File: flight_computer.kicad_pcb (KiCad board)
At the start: 2 copper layers, 43 x 60 mm, 10 parts, among them J1 Conn_01x13_Socket, J2 Conn_01x13_Socket, J3 Ignitor Output, J4 9v Battery Input, U1 CPC1002N, U2 CPC1002N, U3 CPC1002N

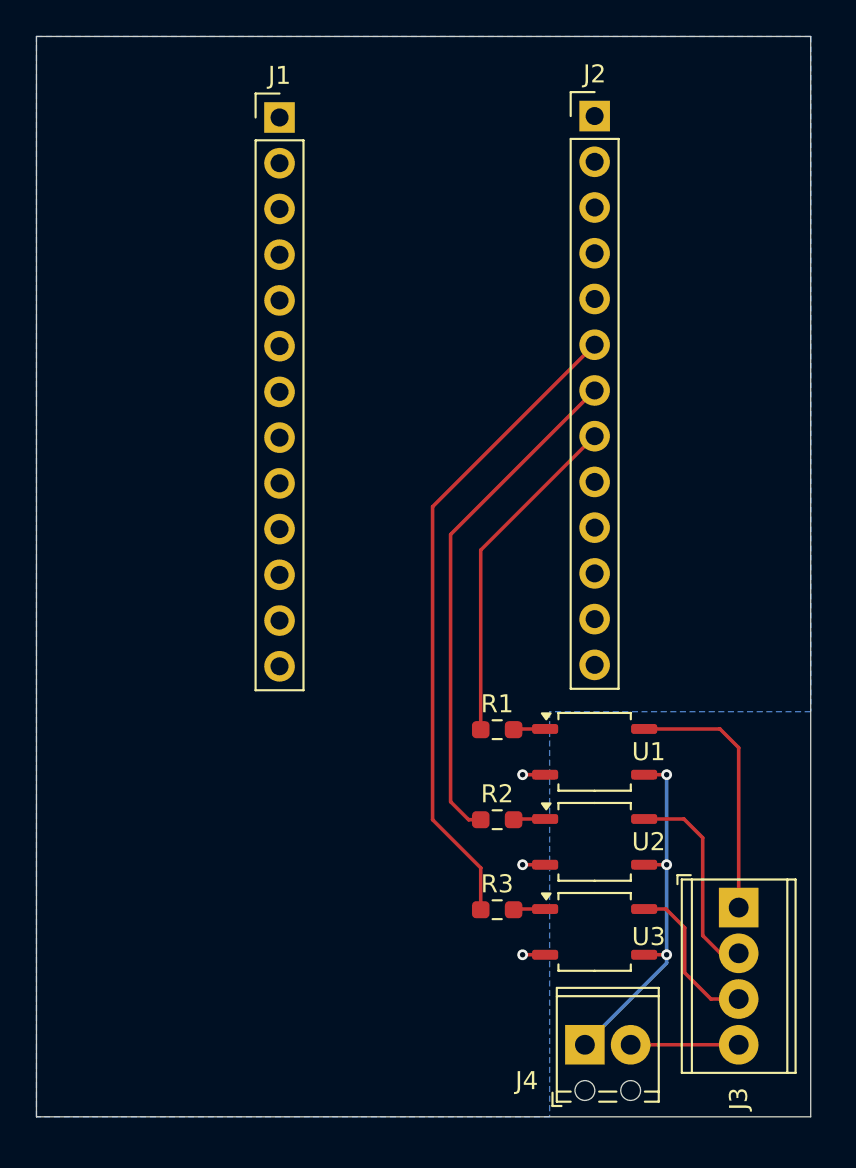
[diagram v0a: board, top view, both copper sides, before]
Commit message: Layout finished for BNO055 and BME280
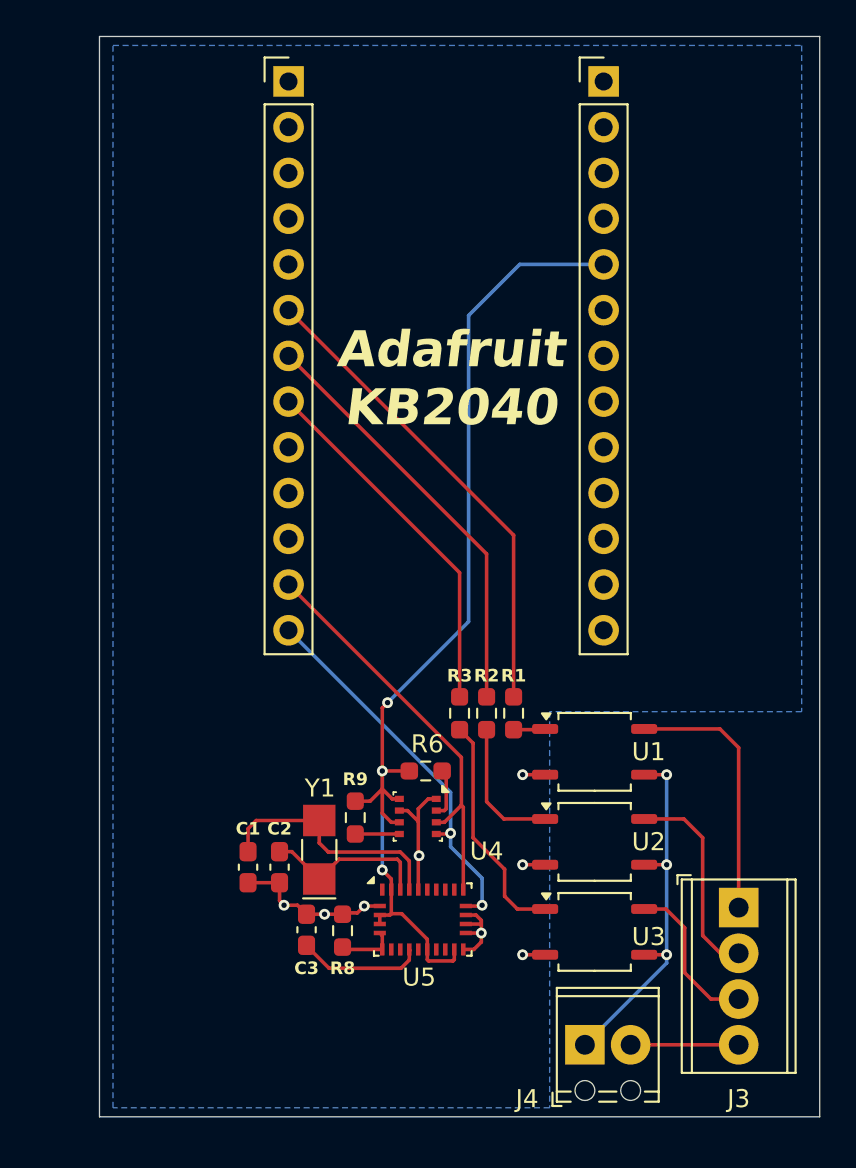
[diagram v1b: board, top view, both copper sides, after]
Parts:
- added C1: 22pF, Capacitor_SMD:C_0603_1608Metric_Pad1.08x0.95mm_HandSolder, F.Cu at (96.8, 104.6)
- added C2: 22pF, Capacitor_SMD:C_0603_1608Metric_Pad1.08x0.95mm_HandSolder, F.Cu at (98.5, 104.6)
- added C3: 0.1µF, Capacitor_SMD:C_0603_1608Metric_Pad1.08x0.95mm_HandSolder, F.Cu at (100.0, 108.1)
- added R6: 10k, Resistor_SMD:R_0603_1608Metric_Pad0.98x0.95mm_HandSolder, F.Cu at (106.6, 99.3)
- added R8: 10k, Resistor_SMD:R_0603_1608Metric_Pad0.98x0.95mm_HandSolder, F.Cu at (102.0, 108.2)
- added R9: 10k, Resistor_SMD:R_0603_1608Metric_Pad0.98x0.95mm_HandSolder, F.Cu at (102.7, 101.9)
- added U4: BME280, Package_LGA:Bosch_LGA-8_2.5x2.5mm_P0.65mm_ClockwisePinNumbering, F.Cu at (106.2, 101.8)
- added U5: BNO055, Package_LGA:LGA-28_5.2x3.8mm_P0.5mm, F.Cu at (106.5, 107.5)
- added Y1: 33.768kHz, Crystal:Crystal_SMD_G8-2Pin_3.2x1.5mm_HandSoldering, F.Cu at (100.7, 103.7)
- moved J1 18.1 mm to (116.5, 61.0)
- moved J2 17.1 mm to (99.0, 61.0)
- moved R3 11.1 mm to (108.5, 96.1), turned to -90 degrees
- moved R2 5.94 mm to (110.0, 96.1), turned to -90 degrees
- moved R1 1.29 mm to (111.5, 96.1), turned to -90 degrees
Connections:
- net Ignitor Logic 2 + renamed /Ignitor Logic 2 +
- net Ignitor Terminal 1 renamed /Ignitor Terminal 1
- net Ignitor Terminal 2 renamed /Ignitor Terminal 2
- net Ignitor Terminal 3 renamed /Ignitor Terminal 3
- net Ignitor Terminal Common renamed /Ignitor Terminal GND
- J1 pad 5: unconnected-(J1-Pin_5-Pad5) -> +3.3V
- J2 pad 12: unconnected-(J2-Pin_12-Pad12) -> /SDA
- J2 pad 13: unconnected-(J2-Pin_13-Pad13) -> /SCL
- J2 pad 6: Ignitor Logic 3 + -> /Ignitor Logic 1 +
- J2 pad 8: Ignitor Logic 1 + -> /Ignitor Logic 3 +
- R1 pad 1: Ignitor Logic 1 + -> /Ignitor Logic 1 +
- R3 pad 1: Ignitor Logic 3 + -> /Ignitor Logic 3 +
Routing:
- net +3.3V: track 0.00 -> 59.1 mm, vias 0 -> 3
- net Ignitor Logic 3 +: track 36.2 -> 0.00 mm
- net /Ignitor Logic 1 +: track 0.00 -> 26.7 mm
- net /SDA: track 0.00 -> 22.7 mm
- net /SCL: track 0.00 -> 21.5 mm, vias 0 -> 2
- net GND: track 3.75 -> 24.7 mm, vias 3 -> 8
- net /Ignitor Logic 3 +: track 0.00 -> 20.3 mm
- net Ignitor Logic 1 +: track 18.9 -> 0.00 mm
- net Net-(U5-XOUT32): track 0.00 -> 13.7 mm
- net Net-(R3-Pad2): track 1.77 -> 12.9 mm
- net Net-(U5-XIN32): track 0.00 -> 9.38 mm
- net Net-(U5-CAP): track 0.00 -> 7.09 mm
- net Net-(R2-Pad2): track 1.77 -> 7.70 mm
- net /Ignitor Logic 2 +: track 28.2 -> 23.5 mm
- net Net-(U5-PS0): track 0.00 -> 3.30 mm
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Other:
- board size 43 x 60 mm -> 40 x 60 mm
- board text added: "Adafruit KB2040"

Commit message: Completed sensor layout
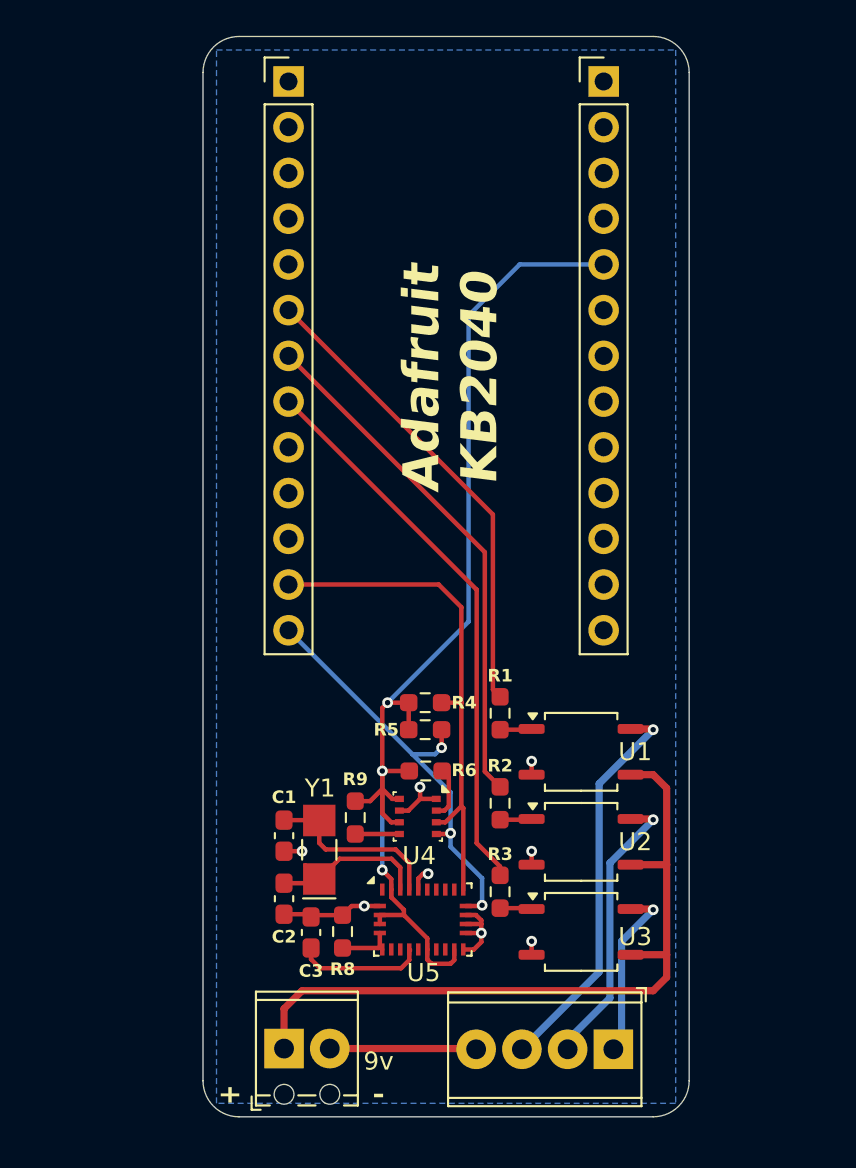
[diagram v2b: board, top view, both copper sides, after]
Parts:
- added R4: 4.4k, Resistor_SMD:R_0603_1608Metric_Pad0.98x0.95mm_HandSolder, F.Cu at (106.6, 95.5)
- added R5: 4.4k, Resistor_SMD:R_0603_1608Metric_Pad0.98x0.95mm_HandSolder, F.Cu at (106.6, 97.0)
- moved J4 16.7 mm to (98.8, 114.7)
- moved J3 10.5 mm to (117.0, 114.8), turned to 180 degrees
- moved R3 10.2 mm to (110.8, 106.0)
- moved R2 5.06 mm to (110.8, 101.1)
- moved C1 2.66 mm to (98.8, 102.9)
- moved C2 1.77 mm to (98.8, 106.4)
- moved R1 0.75 mm to (110.8, 96.1)
- moved U1 0.75 mm to (115.2, 98.2)
- moved U2 0.75 mm to (115.2, 103.2)
- moved U3 0.75 mm to (115.2, 108.2)
- moved C3 0.29 mm to (100.2, 108.3)
- moved R8 0.05 mm to (102.0, 108.2)
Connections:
- net /Ignitor Terminal GND renamed /Ignitor Terminal +
- J3 pad 1: /Ignitor Terminal 1 -> /Ignitor Terminal 3
- J3 pad 3: /Ignitor Terminal 3 -> /Ignitor Terminal 1
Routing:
- net /Ignitor Terminal +: track 16.9 -> 41.0 mm, vias 3 -> 0
- net Net-(R3-Pad2): track 12.9 -> 1.77 mm
- net /Ignitor Logic 3 +: track 20.3 -> 31.2 mm
- net /Ignitor Terminal 1: track 14.6 -> 22.0 mm, vias 0 -> 1
- net GND: track 24.7 -> 18.2 mm
- net /SDA: track 22.7 -> 28.7 mm
- net Net-(R2-Pad2): track 7.70 -> 1.77 mm
- net /Ignitor Logic 2 +: track 23.5 -> 28.8 mm
- net /Ignitor Terminal 2: track 11.5 -> 16.0 mm, vias 0 -> 1
- net Net-(U5-XOUT32): track 13.7 -> 10.1 mm
- net +3.3V: track 59.1 -> 62.2 mm
- net /SCL: track 21.5 -> 24.2 mm, vias 2 -> 3
- net Net-(J3-Pin_4): track 6.00 -> 8.15 mm
- net /Ignitor Terminal 3: track 8.79 -> 9.93 mm, vias 0 -> 1
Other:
- board size 40 x 60 mm -> 27 x 60 mm
- board text added: "+"
- board text added: "-"
- board text added: "9v"
- board text added: "Revision: 0.1.0"
- board text added: "UNL Aerospace Flight Computer"

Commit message: Added voltage regulator
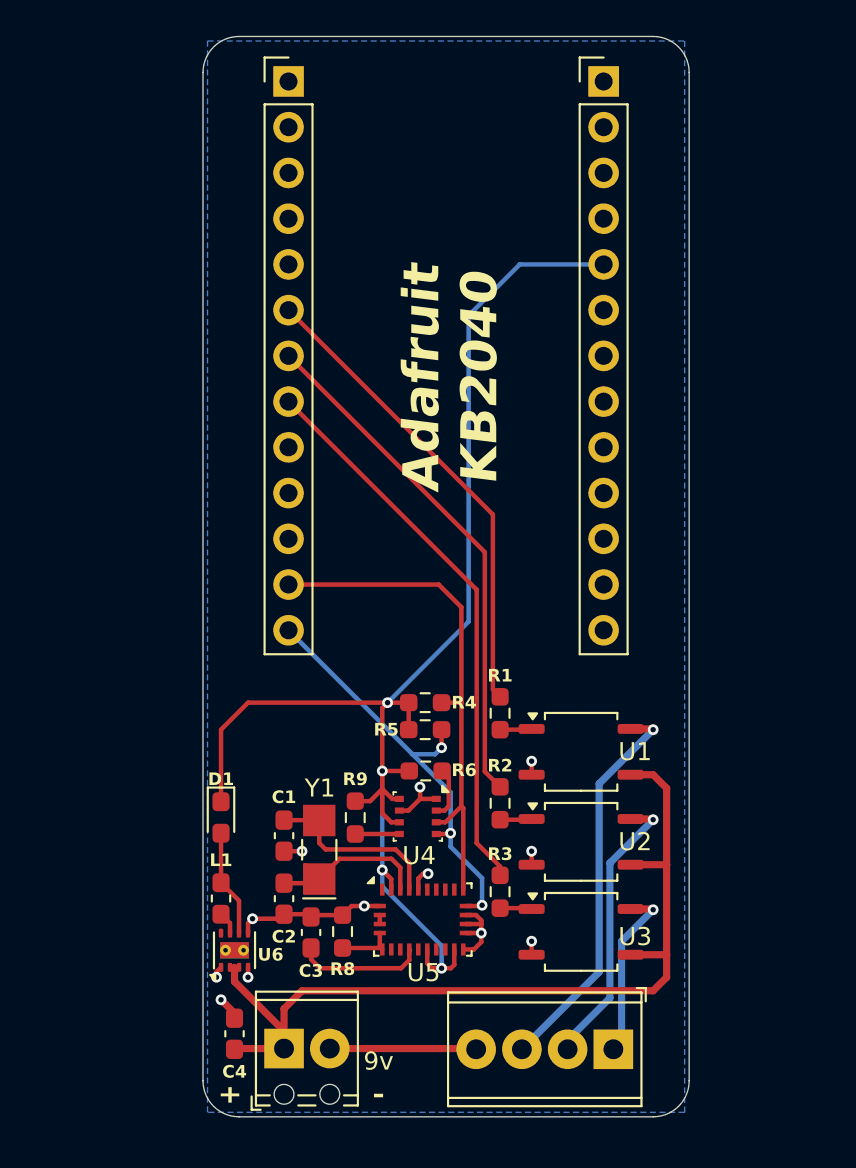
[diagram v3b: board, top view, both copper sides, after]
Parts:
- added C4: 10µF, Capacitor_SMD:C_0603_1608Metric_Pad1.08x0.95mm_HandSolder, F.Cu at (96.0, 113.9)
- added D1: D, Diode_SMD:D_0603_1608Metric_Pad1.05x0.95mm_HandSolder, F.Cu at (95.2, 101.9)
- added L1: 2.2µH, Inductor_SMD:L_0603_1608Metric_Pad1.05x0.95mm_HandSolder, F.Cu at (95.2, 106.4)
- added U6: TPS62172DSG, Package_SON:WSON-8-1EP_2x2mm_P0.5mm_EP0.9x1.6mm_ThermalVias, F.Cu at (96.0, 109.2)
- J4: value 9v Battery Input -> Battery Input
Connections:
- net /Ignitor Terminal + renamed +BATT
- J1 pad 2: unconnected-(J1-Pin_2-Pad2) -> +3.3V
- J1 pad 5: +3.3V -> unconnected-(J1-Pin_5-Pad5)
- J3 pad 4: Net-(J3-Pin_4) -> GND
- J4 pad 2: Net-(J3-Pin_4) -> GND
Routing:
- net +3.3V: track 62.2 -> 77.7 mm, vias 3 -> 4
- net GND: track 18.2 -> 31.7 mm, vias 8 -> 12
- net +BATT: track 41.0 -> 49.9 mm
- net Net-(J3-Pin_4): track 8.15 -> 0.00 mm
- net Net-(D1-A): track 0.00 -> 6.21 mm
- net Net-(U6-SW): track 0.00 -> 1.26 mm

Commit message: Improved layout of connectors
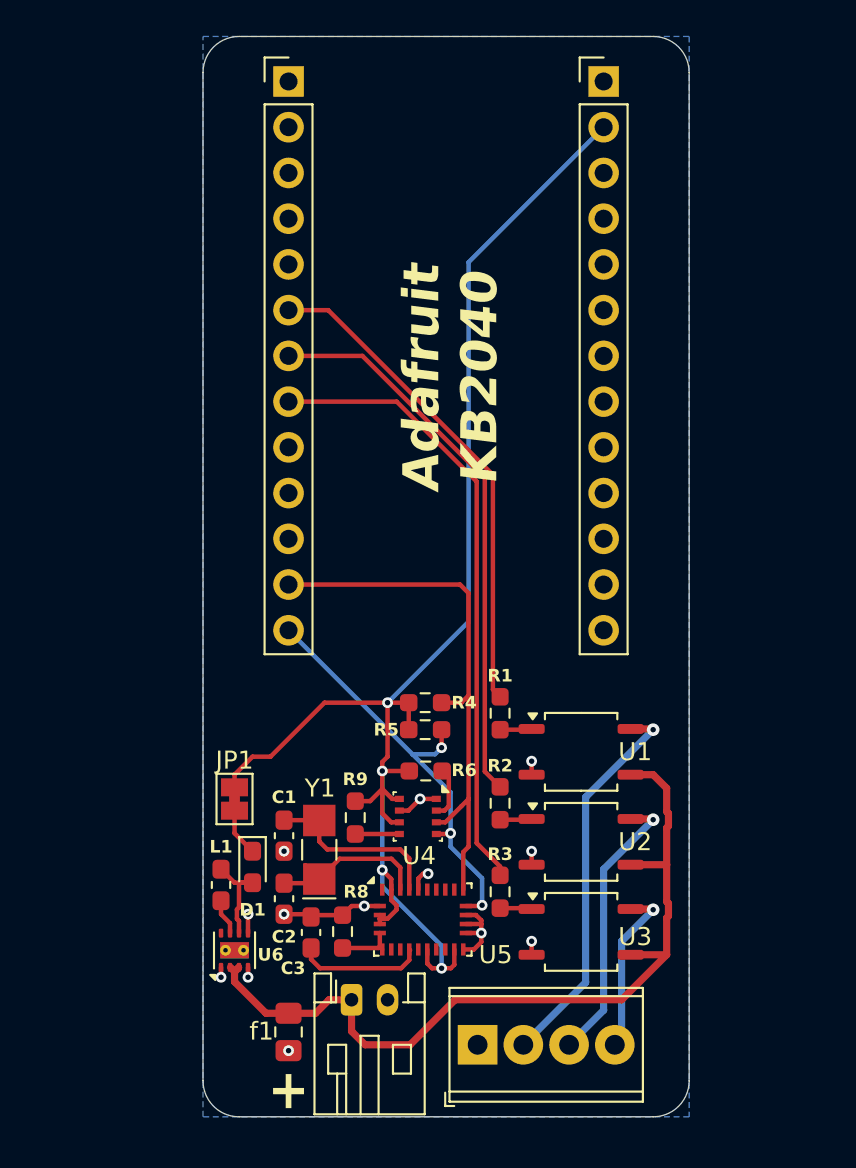
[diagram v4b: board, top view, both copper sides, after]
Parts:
- removed C4: 10µF, Capacitor_SMD:C_0603_1608Metric_Pad1.08x0.95mm_HandSolder
- removed J4: Battery Input, TerminalBlock_Phoenix:TerminalBlock_Phoenix_MPT-0,5-2-2.54_1x02_P2.54mm_Horizontal
- added J5: Battery Input, Connector_JST:JST_PH_S2B-PH-K_1x02_P2.00mm_Horizontal, F.Cu at (102.5, 112.0)
- added JP1: Battery, Jumper:SolderJumper-2_P1.3mm_Bridged_Pad1.0x1.5mm, F.Cu at (96.0, 100.8)
- added f1: 10µF, Capacitor_SMD:C_0805_2012Metric_Pad1.18x1.45mm_HandSolder, F.Cu at (99.0, 113.8)
- moved J3 7.54 mm to (109.5, 114.5), turned to 0 degrees
- moved D1 3.26 mm to (97.0, 104.6)
- moved L1 0.75 mm to (95.2, 105.6)
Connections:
- D1 pad 1: +3.3V -> Net-(D1-K)
- J3 pad 1: /Ignitor Terminal 3 -> GND
- J3 pad 2: /Ignitor Terminal 2 -> /Ignitor Terminal 1
- J3 pad 3: /Ignitor Terminal 1 -> /Ignitor Terminal 2
- J3 pad 4: GND -> /Ignitor Terminal 3
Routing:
- net GND: track 31.7 -> 18.7 mm, vias 12 -> 13
- net +3.3V: track 77.7 -> 82.2 mm
- net +BATT: track 49.9 -> 46.4 mm
- net /Ignitor Logic 3 +: track 31.2 -> 34.7 mm
- net Net-(D1-K): track 0.00 -> 2.66 mm
- net /Ignitor Logic 2 +: track 28.8 -> 31.2 mm
- net /SDA: track 28.7 -> 30.8 mm
- net /Ignitor Logic 1 +: track 26.3 -> 27.6 mm
- net Net-(U6-SW): track 1.26 -> 2.01 mm
- net Net-(D1-A): track 6.21 -> 5.71 mm
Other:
- board text removed: "9v"

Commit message: Added MicroSD card slot
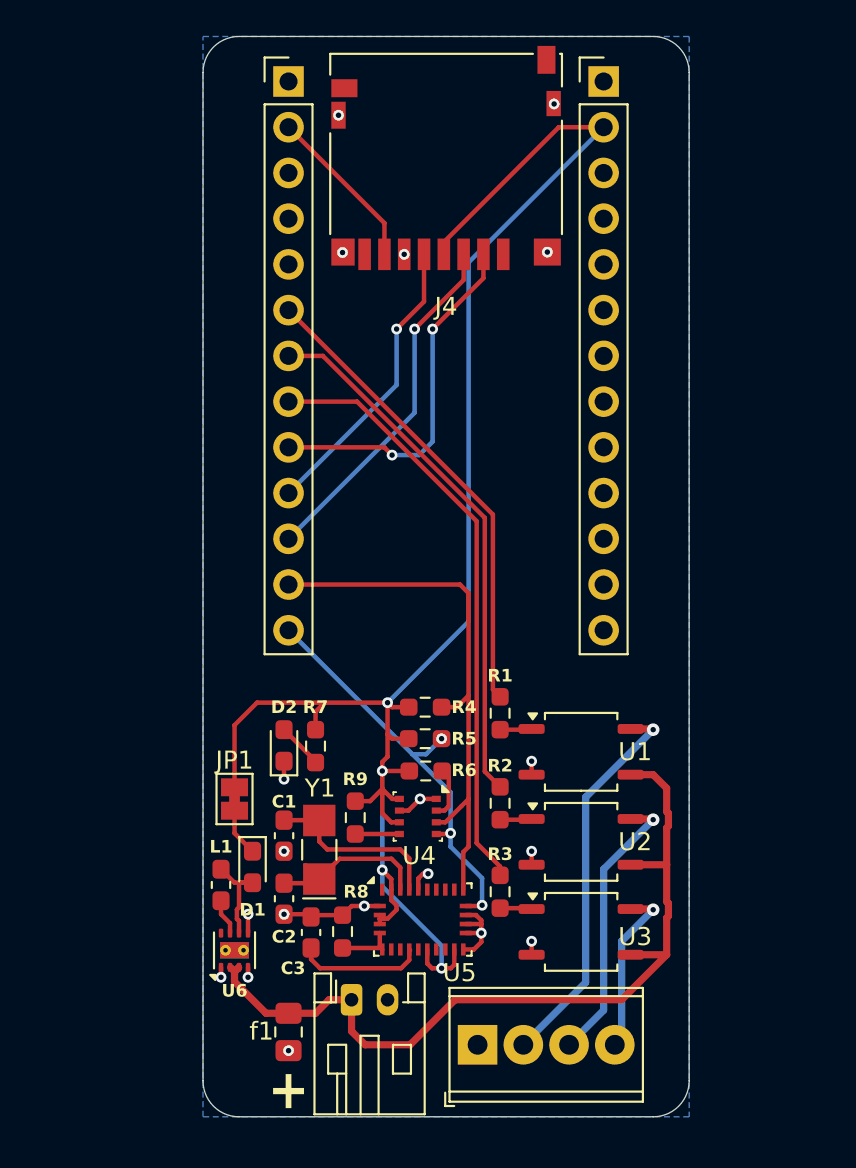
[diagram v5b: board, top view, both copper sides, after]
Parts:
- added D2: LED, LED_SMD:LED_0603_1608Metric_Pad1.05x0.95mm_HandSolder, F.Cu at (98.8, 97.9)
- added J4: Micro_SD_Card, Connector_Card:microSD_HC_Hirose_DM3D-SF, F.Cu at (107.8, 65.2)
- added R7: 4.4k, Resistor_SMD:R_0603_1608Metric_Pad0.98x0.95mm_HandSolder, F.Cu at (100.5, 97.9)
- moved R5 0.50 mm to (106.6, 97.5)
- moved R4 0.25 mm to (106.6, 95.8)
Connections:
- J2 pad 10: unconnected-(J2-Pin_10-Pad10) -> /SPI SCK
- J2 pad 11: unconnected-(J2-Pin_11-Pad11) -> /SPI SDO
- J2 pad 2: unconnected-(J2-Pin_2-Pad2) -> /SPI SDI
- J2 pad 9: unconnected-(J2-Pin_9-Pad9) -> /SPI CS
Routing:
- net /SPI CS: track 0.00 -> 20.1 mm, vias 0 -> 2
- net /SPI SDO: track 0.00 -> 19.8 mm, vias 0 -> 1
- net /SPI SCK: track 0.00 -> 16.4 mm, vias 0 -> 1
- net +3.3V: track 82.2 -> 97.6 mm
- net /SPI SDI: track 0.00 -> 9.27 mm
- net Net-(D2-A): track 0.00 -> 2.55 mm
- net /Ignitor Logic 2 +: track 31.2 -> 29.9 mm
- net /Ignitor Logic 1 +: track 27.6 -> 26.3 mm
- net /Ignitor Logic 3 +: track 34.7 -> 33.4 mm
- net GND: track 18.7 -> 20.0 mm, vias 13 -> 19
- net /SCL: track 24.2 -> 23.4 mm
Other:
- board text added: "Grant G. - https://g2games.dev/"
- board text added: "Specs: • 3 flight events • 3-16v input • Data logging • Altitude • Pressure • Temperature • 9DoF Spatial orientation"
- board text added: "WARNING: Do NOT power with USB and battery simultaneously It WILL break"
- board text removed: "Adafruit KB2040"
- board text removed: "UNL Aerospace Flight Computer"
